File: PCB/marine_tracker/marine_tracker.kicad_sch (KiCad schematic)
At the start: 0 parts

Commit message: STM32 Schematic finished
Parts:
- added C1: 4.7u, Capacitor_SMD:C_0805_2012Metric, symbol Device:C
- added C10, C3, C4, C5, C8, C9: 100n, Capacitor_SMD:C_01005_0402Metric, symbol Device:C
- added C11, C12: 10p, Capacitor_SMD:C_0402_1005Metric, symbol Device:C
- added C13, C14: 20p, Capacitor_SMD:C_0402_1005Metric, symbol Device:C
- added C2: 10u, Capacitor_SMD:C_0805_2012Metric, symbol Device:C
- added C6, C7: 1u, Capacitor_SMD:C_0201_0603Metric, symbol Device:C
- added J1: ST LINK V2 Connector, Connector_PinHeader_2.54mm:PinHeader_2x10_P2.54mm_Vertical, symbol Connector:Conn_ARM_JTAG_SWD_20
- added R1, R2, R3, R4: 10k, Resistor_SMD:R_0402_1005Metric, symbol Device:R
- added SW1: SW_Push, Button_Switch_SMD:SW_Tactile_SPST_NO_Straight_CK_PTS636Sx25SMTRLFS, symbol Switch:SW_Push
- added U1: STM32U575RGT6, Package_QFP:LQFP-64_10x10mm_P0.5mm, symbol MCU_ST_STM32U5:STM32U575RGTx
- added U2: SHT4x, Sensor_Humidity:Sensirion_DFN-4_1.5x1.5mm_P0.8mm_SHT4x_NoCentralPad, symbol Sensor_Humidity:SHT4x
- added Y1: 32kHz768, Crystal:Crystal_SMD_3215-2Pin_3.2x1.5mm, symbol Device:Crystal
- added Y3: 16MHz, Crystal:Crystal_SMD_5032-4Pin_5.0x3.2mm, symbol Device:Crystal_GND24
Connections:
- new net: C1.1, U1.30 (VCAP)
- new net: J1.11 (RTCK), R4.1
- new net: J1.17 (DBGRQ/NC), R2.1
- new net: J1.19 (DBGACK/NC), R3.1
- new net +3V3: C2.1, C3.1, C4.1, C5.1, C6.1, C7.1, C8.1, C9.1, J1.1 (VTREF), J1.2 (VCC/NC), SW1.1, U1.1 (VBAT), U1.13 (VDDA), U1.19 (VDD), U1.32 (VDD), U1.48 (VDDUSB), U1.64 (VDD)
- new net BOOT0: R1.1, SW1.2, U1.60 (PH3)
- new net GND: C1.2, C10.2, C11.1, C12.1, C13.1, C14.1, C2.2, C3.2, C4.2, C5.2, C6.2, C7.2, C8.2, C9.2, J1.10 (GND), J1.12 (GND), J1.14 (GND), J1.16 (GND), J1.18 (GND), J1.20 (GND), J1.4 (GND), J1.6 (GND), J1.8 (GND), R1.2, R2.2, R3.2, R4.2, U1.12 (VSSA), U1.18 (VSS), U1.31 (VSS), U1.47 (VSS), U1.63 (VSS), Y3.4 (G)
- new net HSE_IN: C13.2, U1.5 (PH0), Y3.1
- new net HSE_OUT: C14.2, U1.6 (PH1), Y3.3
- new net JTDI: J1.5 (TDI), U1.50 (PA15)
- new net LSE_IN: C11.2, U1.3 (PC14), Y1.1
- new net LSE_OUT: C12.2, U1.4 (PC15), Y1.2
- new net SWCLK: J1.9 (SWCLK), U1.49 (PA14)
- new net SWDIO: J1.7 (SWDIO), U1.46 (PA13)
- new net SWD_NRST: C10.1, J1.15 (~{SRST}), U1.7 (NRST)
- new net SWO: J1.13 (SWO), U1.55 (PB3)
- new net TRST: J1.3 (~{TRST}), U1.56 (PB4)
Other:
- note added: "C11 = C12 = 2*(CL - 5pF) = 2*(10pF - 5pF) = 10pF"
- note added: "C13 = C14 = 2*(CL - 5pF) = 2*(15pF - 5pF) = 20pF"
- company: (none) -> HES-SO
- title: (none) -> Marine Tracker

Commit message: update schematics
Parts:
- removed J1: ST LINK V2 Connector, Connector_PinHeader_2.54mm:PinHeader_2x10_P2.54mm_Vertical, symbol Connector:Conn_ARM_JTAG_SWD_20
- removed R2, R3, R4: 10k, Resistor_SMD:R_0402_1005Metric, symbol Device:R
- added AE1: Antenna, symbol Device:Antenna
- added BT1: Battery_Cell, symbol Device:Battery_Cell
- added C15, C16: 1u, Capacitor_SMD:C_0201_0603Metric, symbol Device:C
- added C17: 100n, Capacitor_SMD:C_01005_0402Metric, symbol Device:C
- added C18, C19: 10u, Capacitor_SMD:C_0805_2012Metric, symbol Device:C
- added J2: Conn_ARM_JTAG_SWD_10, Connector_PinHeader_1.27mm:PinHeader_2x05_P1.27mm_Vertical, symbol Connector:Conn_ARM_JTAG_SWD_10
- added R5, R6: 10k, Resistor_SMD:R_0402_1005Metric, symbol Device:R
- added U3: AST50147-xx, RF_Module:Astrocast_AST50147-00, symbol RF_Module:AST50147-xx
- added U4: MIC5504-3.3YM5, Package_TO_SOT_SMD:SOT-23-5, symbol Regulator_Linear:MIC5504-3.3YM5
- added U5: SAM-M10Q, Beuns_PCBFootprint:XCVR_SAM-M10Q-00B, symbol BeunsLibrary:SAM-M10Q
- U2: value SHT4x -> SHT40
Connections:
- net +3V3: now also U2.3 (VDD), C16.1, C17.1, C18.1, C19.1, J2.1 (VTref), R5.1, R6.1, U3.1 (VDD), U3.2 (VDD), U4.5 (VOUT), U5.17 (VCC), U5.2 (V_IO)
- net GND: now also U2.4 (VSS), BT1.2 (-), C15.2, C16.2, C17.2, C18.2, C19.2, J2.3 (GND), J2.5 (GND), J2.9 (GNDDetect), U3.11 (GND), U3.13 (GND), U3.15 (GND_RF), U3.16 (GND_RF), U3.18 (GND_RF), U3.19 (GND_RF), U3.23 (GND), U3.25 (GND), U3.27 (GND), U3.29 (GND), U3.3 (GND), U3.31 (GND), U3.33 (GND), U3.36 (GND), U3.5 (GND), U3.7 (GND), U3.9 (GND), U4.2 (GND), U5.1 (GND), U5.10 (GND), U5.11 (GND), U5.15 (GND), U5.16 (GND), U5.20 (GND), U5.4 (GND), U5.5 (GND), U5.6 (GND)
- net SWCLK: now also J2.4 (SWCLK/TCK)
- net SWDIO: now also J2.2 (SWDIO/TMS)
- net SWD_NRST: now also J2.10 (~{RESET})
- net I2C1_SDA: now reaches U2.1 (SDA)
- net I2C1_SDA: now also U1.59 (PB7), R6.2
- net I2C1_SCL: now reaches U2.2 (SCL)
- net I2C1_SCL: now also U1.58 (PB6), R5.2
- net AST_RXD: now reaches U1.16 (PA2)
- net AST_RXD: now also U3.12 (RXD)
- net AST_TXD: now reaches U1.17 (PA3)
- net AST_TXD: now also U3.10 (TXD)
- net VCAP: now reaches C1.1, U1.30 (VCAP)
- net JTDI: no longer names the net of U1.50 (PA15)
- net SWO: no longer names the net of U1.55 (PB3)
- net TRST: no longer names the net of U1.56 (PB4)
- new net: AE1.1 (A), U3.17 (ANTN_RF)
- new net +BATT: BT1.1 (+), C15.1, U4.1 (VIN), U4.3 (EN)
- new net AST_ANTUSE: U3.6 (ANTN_USE)
- new net AST_EVENT: U3.4 (EVENT_NOTIF)
- new net AST_RST: U3.14 (RESET)
- new net AST_WAKEUP: U3.8 (WAKEUP)
- new net GPS_EXTINT: U5.19 (EXTINT)
- new net GPS_N_RST: U5.18 (RESET_N)
- new net GPS_PULSE: U5.7 (TIMEPULSE)
- new net GPS_RXD: U5.14 (RXD)
- new net GPS_TXD: U5.13 (TXD)
- no-connect marks 0 -> 5
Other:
- note added: "1S full : (4.2V - 3.3V) x 100mA = 90 mW 2S full : (8.4V - 3.3V) x 100mA = 510 mW"
- note added: "BOOT0 Switch"
- note added: "Capacitance for Crystal Oscillator"
- note added: "HSE : C13 = C14 = 2*(CL - 5pF) = 2*(15pF - 5pF) = 20pF"
- note added: "Input range : 2.5V to 5.5V Output : 3.3V Output current : 300mA"
- note added: "LDO Characteristics"
- note added: "LSE : C11 = C12 = 2*(CL - 5pF) = 2*(10pF - 5pF) = 10pF"
- note added: "LiPo 1S (3.5V-4.2V) to 3.3V LDO"
- note added: "Low power satellite communication module"
- note added: "Patch antenna"
- note added: "Pinout - TIMEPULSE pin: Precise GNSS-synchronized clock output (typically 1PPS) - EXTINT pin: External interrupt input (used for wake-up from low-power modes). Layout requirements (Refer to SAM-M10Q Integration Manual) - Minimum ground plane size: 50mm x 50mm - Minimum clearance: 10mm from each module edges (no components or copper) - Keep supply and digital lines short on the top layer - Use sol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"
- note added: "Power Loss"
- note added: "Precision GNSS receiver with an integrated antenna"
- note added: "RF characteristics - RX frequency range: 1525 - 1559 MHz - TX frequency range: 1626.5 - 1660.5 MHz - Output impedance: 50ohm Layout requirements - Minimum ground plane size: 65mm x 65mm - Minimum clearance: 15mm from PCB edges - Feeding: metalized via (position must follow manufacturer datasheet)"
- note added: "Run mode (SWD) : BOOT0 = 0 Bootloader mode (USB, UART..) : BOOT0 = 1"
- note added: "STM32U5 MCU"
- note added: "SWD connector"
- note added: "Temperature Sensor"
- note removed: "C11 = C12 = 2*(CL - 5pF) = 2*(10pF - 5pF) = 10pF"
- note removed: "C13 = C14 = 2*(CL - 5pF) = 2*(15pF - 5pF) = 20pF"
- company: HES-SO -> Wearable Sensing System Design
- title: Marine Tracker -> Marine Animal Tracking System
- moved on the sheet: U2

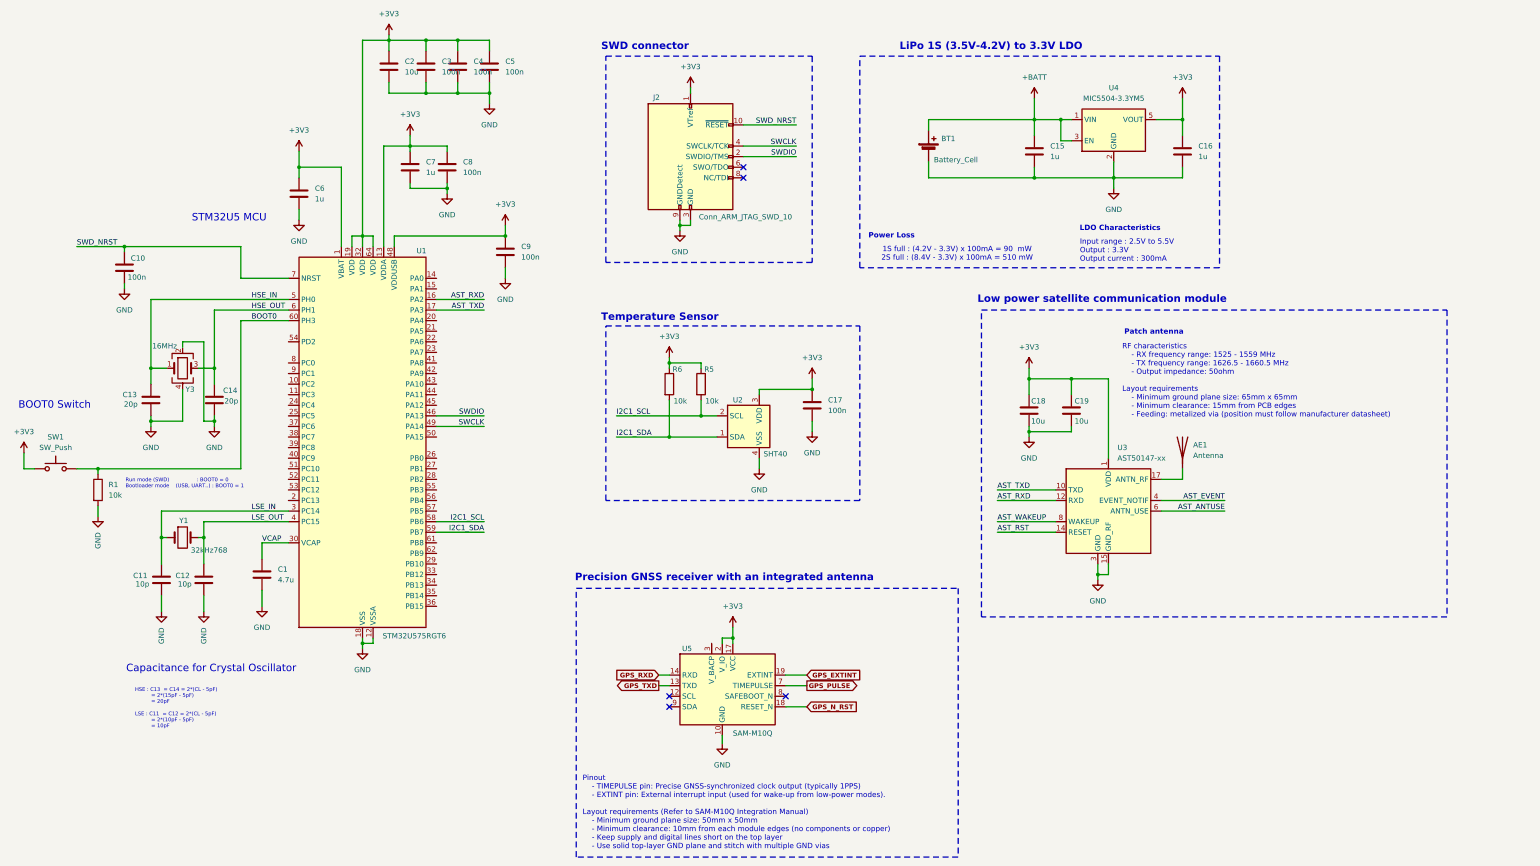
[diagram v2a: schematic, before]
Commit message: schematics update
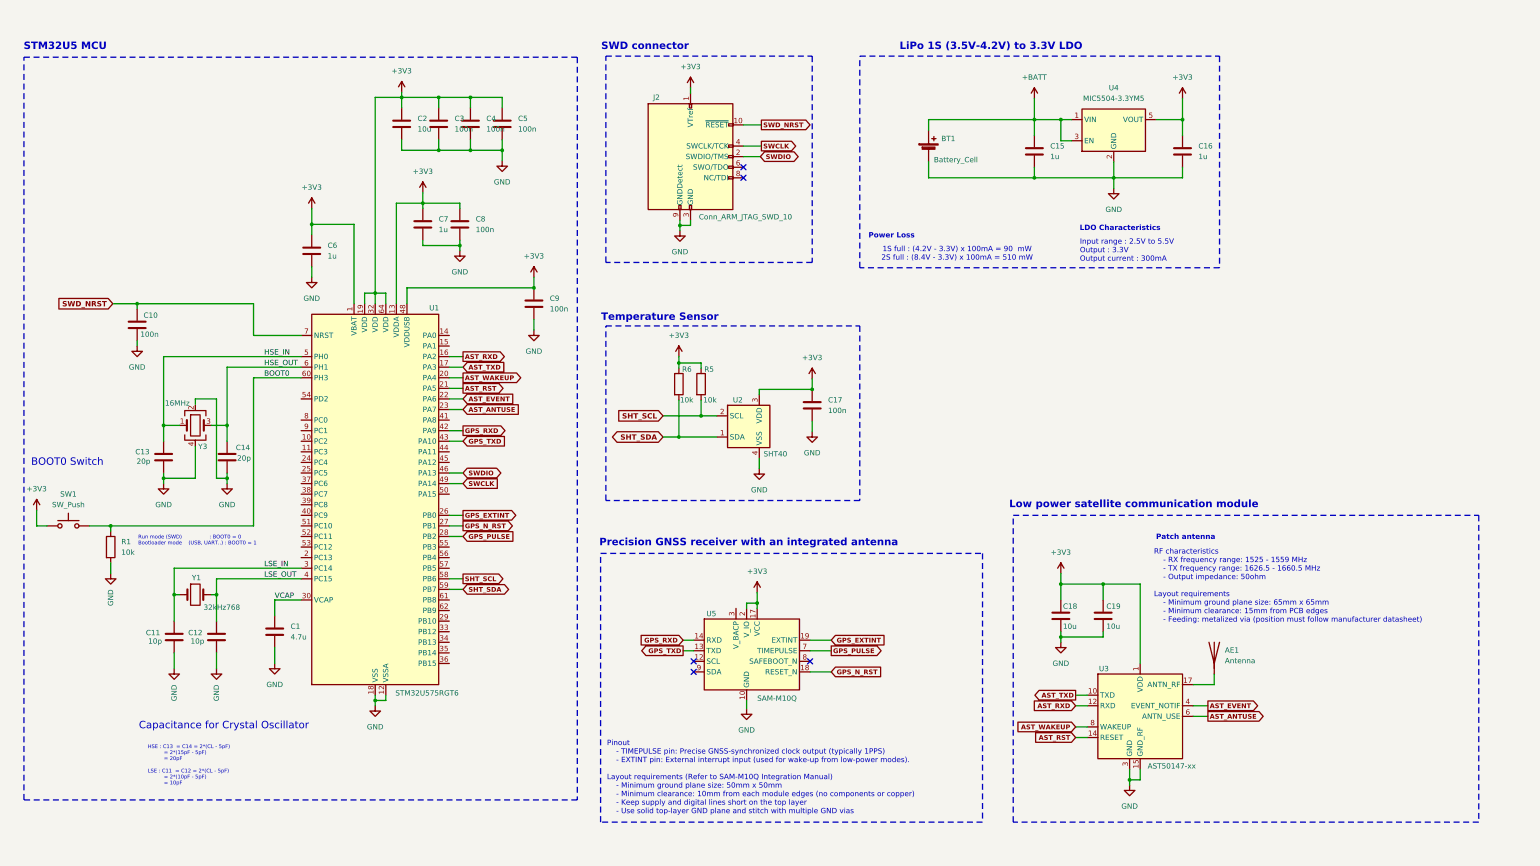
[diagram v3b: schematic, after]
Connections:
- net AST_ANTUSE: now also U1.23 (PA7)
- net AST_EVENT: now also U1.22 (PA6)
- net AST_RST: now also U1.21 (PA5)
- net AST_WAKEUP: now also U1.20 (PA4)
- net GPS_EXTINT: now also U1.26 (PB0)
- net GPS_N_RST: now also U1.27 (PB1)
- net GPS_PULSE: now also U1.28 (PB2)
- net GPS_RXD: now also U1.42 (PA9)
- net GPS_TXD: now also U1.43 (PA10)
- net I2C1_SCL renamed SHT_SCL
- net I2C1_SDA renamed SHT_SDA
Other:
- moved on the sheet: AE1, C1, C10, C11, C12, C13, C14, C18, C19, C2, C3, C4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

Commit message: update schematics
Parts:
- added U6: 25CSM04T-I/SN, Package_SO:SOIC-8-1EP_3.9x4.9mm_P1.27mm_EP2.29x3mm, symbol Memory_EEPROM:25CSM04xxMF
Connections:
- net +3V3: now also U6.8 (V_{CC})
- net GND: now also U6.4 (V_{SS})
- net MEM_SPI1_SCK: now reaches U1.15 (PA1)
- net MEM_SPI1_SCK: now also U6.6 (SCK)
- net MEM_SPI1_MISO: now reaches U1.44 (PA11)
- net MEM_SPI1_MISO: now also U6.2 (SO)
- net MEM_SPI1_MOSI: now reaches U1.45 (PA12)
- net MEM_SPI1_MOSI: now also U6.5 (SI)
- net MEM_SPI1_CS: now reaches U1.50 (PA15)
- net MEM_SPI1_CS: now also U6.1 (~{CS})
- net MEM_HOLD: now reaches U1.55 (PB3)
- net MEM_HOLD: now also U6.7 (~{HOLD})
- no-connect marks 5 -> 33
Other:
- note added: "1. Battery connector 2. Pressure sensor connector 3. Antenna"
- note added: "500kB SPI Serial EEPROM"
- note added: "TO DO"
- note removed: "1S full : (4.2V - 3.3V) x 100mA = 90 mW 2S full : (8.4V - 3.3V) x 100mA = 510 mW"
- note removed: "Power Loss"

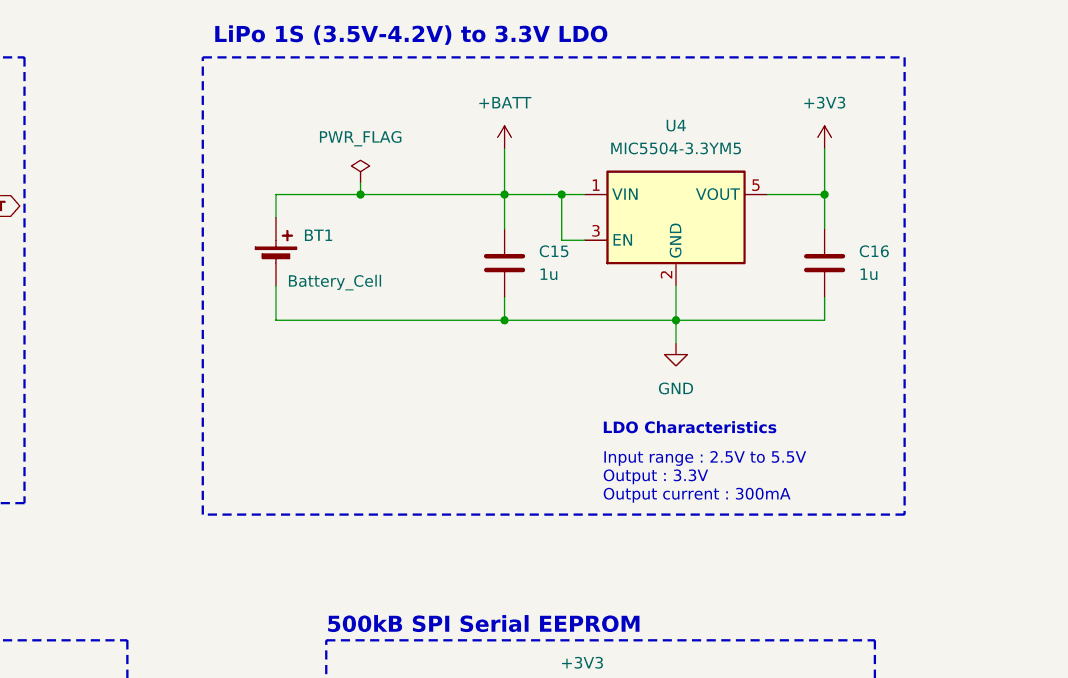
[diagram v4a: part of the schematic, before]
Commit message: add screw terminal for battery
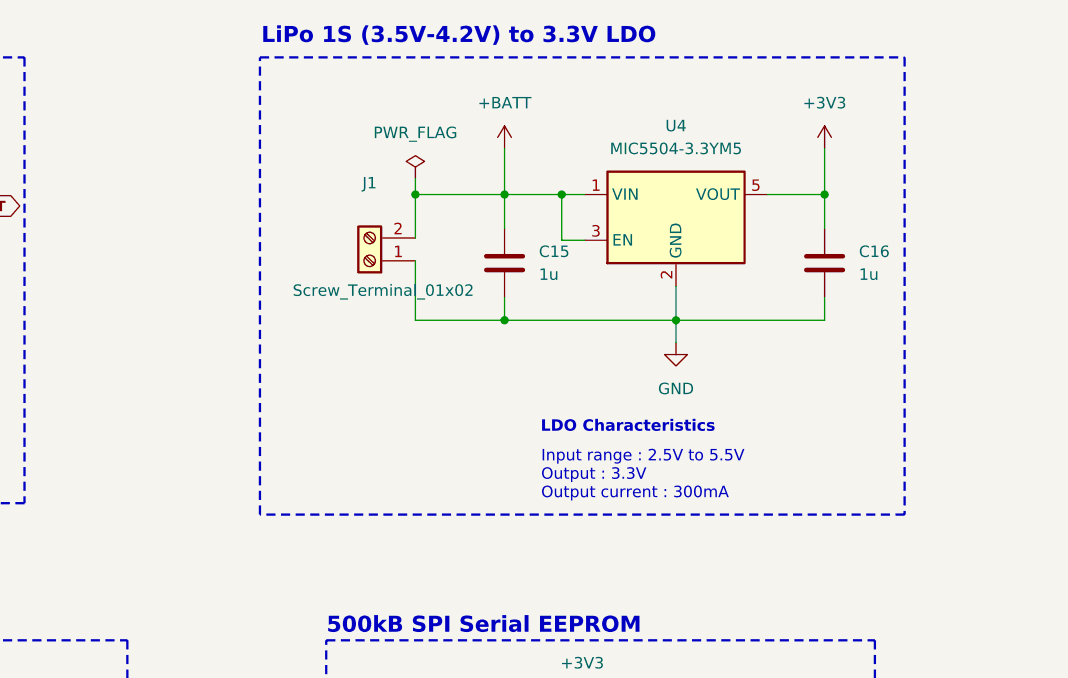
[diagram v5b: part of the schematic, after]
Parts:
- removed BT1: Battery_Cell, symbol Device:Battery_Cell
- added J1: Screw_Terminal_01x02, Beuns_PCBFootprint:Screw_terminal_1x2, symbol Connector:Screw_Terminal_01x02
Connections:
- net +BATT: now also J1.2 (Pin_2)
- net GND: now also J1.1 (Pin_1)
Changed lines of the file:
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@@
 	)
 	(rectangle
-		(start 225.552 27.94)
+		(start 231.902 27.94)
 		(end 303.53 78.74)
 		(stroke
@@
 	(text "LiPo 1S (3.5V-4.2V) to 3.3V LDO"
 		(exclude_from_sim no)
-		(at 248.666 25.654 0)
+		(at 254 25.654 0)
 		(effects
 			(font
@@
 	(text "LDO Characteristics"
 		(exclude_from_sim no)
-		(at 279.654 69.342 0)
+		(at 272.796 69.088 0)
 		(effects
 			(font
@@
 	(text "Input range : 2.5V to 5.5V\nOutput : 3.3V\nOutput current : 300mA"
 		(exclude_from_sim no)
-		(at 270.002 74.676 0)
+		(at 263.144 74.422 0)
 		(effects
 			(font
@@
 	)
 	(junction
-		(at 243.078 43.18)
-		(diameter 0)
-		(color 0 0 0 0)
-	)
-	(junction
 		(at 100.838 183.134)
 		(diameter 0)
@@
 	)
 	(junction
+		(at 249.174 43.18)
+		(diameter 0)
+		(color 0 0 0 0)
+	)
+	(junction
 		(at 123.698 37.846)
 		(diameter 0)
@@
 	(wire
 		(pts
+			(xy 249.174 43.18) (xy 259.08 43.18)
+		)
+		(stroke
+			(width 0)
+			(type default)
+		)
+	)
+	(wire
+		(pts
 			(xy 277.876 108.966) (xy 280.67 108.966)
 		)
@@
 	(wire
 		(pts
-			(xy 243.078 41.91) (xy 243.078 43.18)
+			(xy 249.174 41.402) (xy 249.174 43.18)
 		)
 		(stroke
@@
 	(wire
 		(pts
-			(xy 233.68 45.72) (xy 233.68 43.18)
+			(xy 249.174 50.546) (xy 249.174 57.15)
+		)
+		(stroke
+			(width 0)
+			(type default)
+		)
+	)
+	(wire
+		(pts
+			(xy 249.174 48.006) (xy 249.174 43.18)
 		)
 		(stroke
@@
 	(wire
 		(pts
-			(xy 233.68 57.15) (xy 259.08 57.15)
+			(xy 249.174 57.15) (xy 259.08 57.15)
 		)
 		(stroke
@@
 	(wire
 		(pts
-			(xy 233.68 43.18) (xy 243.078 43.18)
-		)
-		(stroke
-			(width 0)
-			(type default)
-		)
-	)
-	(wire
-		(pts
-			(xy 243.078 43.18) (xy 259.08 43.18)
-		)
-		(stroke
-			(width 0)
-			(type default)
-		)
-	)
-	(wire
-		(pts
 			(xy 174.752 170.688) (xy 177.292 170.688)
 		)
@@
 	(wire
 		(pts
-			(xy 233.68 53.34) (xy 233.68 57.15)
-		)
-		(stroke
-			(width 0)
-			(type default)
-		)
-	)
-	(wire
-		(pts
 			(xy 275.59 154.686) (xy 275.59 158.496)
 		)
@@
 	)
 	(symbol
-		(lib_id "Device:Battery_Cell")
-		(at 233.68 50.8 0)
-		(unit 1)
-		(exclude_from_sim no)
-		(in_bom yes)
-		(on_board yes)
-		(dnp no)
-		(property "Reference" "BT1"
-			(at 236.728 47.752 0)
-			(effects
-				(font
-					(size 1.27 1.27)
-				)
-				(justify left)
-			)
-		)
-		(property "Value" "Battery_Cell"
-			(at 234.95 52.832 0)
-			(effects
-				(font
-					(size 1.27 1.27)
-				)
-				(justify left)
-			)
-		)
-		(property "Footprint" ""
-			(at 233.68 49.276 90)
-			(effects
-				(font
-					(size 1.27 1.27)
-				)
-				(hide yes)
-			)
-		)
-		(property "Datasheet" "~"
-			(at 233.68 49.276 90)
-			(effects
-				(font
-					(size 1.27 1.27)
-				)
-				(hide yes)
-			)
-		)
-		(property "Description" "Single-cell battery"
-			(at 233.68 50.8 0)
-			(effects
-				(font
-					(size 1.27 1.27)
-				)
-				(hide yes)
-			)
-		)
-		(property "Sim.Device" "V"
-			(at 233.68 50.8 0)
-			(effects
-				(font
-					(size 1.27 1.27)
-				)
-				(hide yes)
-			)
-		)
-		(property "Sim.Type" "DC"
-			(at 233.68 50.8 0)
-			(effects
-				(font
-					(size 1.27 1.27)
-				)
-				(hide yes)
-			)
-		)
-		(property "Sim.Pins" "1=+ 2=-"
-			(at 233.68 50.8 0)
-			(effects
-				(font
-					(size 1.27 1.27)
-				)
-				(hide yes)
-			)
-		)
-		(pin "2"
-		)
-		(pin "1"
-		)
-		(instances
-			(project ""
-				(path "/aea3082a-ee68-43bf-ab65-cce2ba7d897e"
-					(reference "BT1")
-					(unit 1)
-				)
-			)
-		)
-	)
-	(symbol
 		(lib_id "power:GND")
 		(at 265.43 168.656 0)
@@
 	(symbol
 		(lib_id "power:PWR_FLAG")
-		(at 243.078 41.91 0)
+		(at 249.174 41.402 0)
 		(unit 1)
 		(exclude_from_sim no)
@@
 		(fields_autoplaced yes)
 		(property "Reference" "#FLG01"
-			(at 243.078 40.005 0)
+			(at 249.174 39.497 0)
 			(effects
 				(font
@@
 		)
 		(property "Value" "PWR_FLAG"
-			(at 243.078 36.83 0)
+			(at 249.174 36.322 0)
 			(effects
 				(font
@@
 		)
 		(property "Footprint" ""
-			(at 243.078 41.91 0)
+			(at 249.174 41.402 0)
 			(effects
 				(font
@@
 		)
 		(property "Datasheet" "~"
-			(at 243.078 41.91 0)
+			(at 249.174 41.402 0)
 			(effects
 				(font
@@
 		)
 		(property "Description" "Special symbol for telling ERC where power comes from"
-			(at 243.078 41.91 0)
+			(at 249.174 41.402 0)
 			(effects
 				(font
@@
 					(unit 1)
 				)
+			)
+		)
+	)
+	(symbol
+		(lib_id "Connector:Screw_Terminal_01x02")
+		(at 244.094 50.546 180)
+		(unit 1)
+		(exclude_from_sim no)
+		(in_bom yes)
+		(on_board yes)
+		(dnp no)
+		(property "Reference" "J1"
+			(at 244.094 41.91 0)
+			(effects
+				(font
+					(size 1.27 1.27)
+				)
+			)
+		)
+		(property "Value" "Screw_Terminal_01x02"
+			(at 245.618 53.848 0)
+			(effects
+				(font
+					(size 1.27 1.27)
+				)
+			)
+		)
+		(property "Footprint" "Beuns_PCBFootprint:Screw_terminal_1x2"
+			(at 244.094 50.546 0)
+			(effects
+				(font
+					(size 1.27 1.27)
+				)
+				(hide yes)
+			)
+		)
+		(property "Datasheet" "https://jlcpcb.com/api/file/downloadByFileSystemAccessId/8588887094307119105"
+			(at 244.094 50.546 0)
+			(effects
+				(font
+					(size 1.27 1.27)
+				)
+				(hide yes)
+			)
+		)
+		(property "Description" "-40℃~+105℃ 1 1.5 14~26 15A 1x2P 2 250V 2P 5mm Green Through Hole Plugin,P=5mm Screw Terminal Blocks ROHS"
+			(at 244.094 50.546 0)
+			(effects
+				(font
+					(size 1.27 1.27)
+				)
+				(hide yes)
+			)
+		)
+		(property "Manufacturer" "Ningbo Kangnex Elec"
+			(at 244.094 50.546 0)
+			(effects
+				(font
+					(size 1.27 1.27)
+				)
+				(hide yes)
+			)
+		)
+		(property "Manufacturer Part Number" "WJ127-5.0-02P-14-00A"
+			(at 244.094 50.546 0)
+			(effects
+				(font
+					(size 1.27 1.27)
+				)
+				(hide yes)
+			)
+		)
+		(property "JLCPCB Part Number" " C3703"
+			(at 244.094 50.546 0)
+			(effects
+				(font
+					(size 1.27 1.27)
+				)
+				(hide yes)
+			)
+		)
+		(pin "1"
+		)
+		(pin "2"
+		)
+		(instances
+			(project ""
+				(path "/aea3082a-ee68-43bf-ab65-cce2ba7d897e"
+					(reference "J1")
+					(unit 1)
+				)
